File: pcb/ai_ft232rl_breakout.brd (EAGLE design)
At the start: 25.4 x 16.3 mm, 14 parts, among them U1 FT232RLSSOP

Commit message: aligned board to origin.
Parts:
- moved C1 35.6 mm to (18.8, 11.9)
- moved C2 35.6 mm to (18.0, 8.89)
- moved C3 35.6 mm to (17.3, 14.5)
- moved JP2 35.6 mm to (6.86, 1.78)
- moved LED1 35.6 mm to (20.1, 10.9)
- moved LED2 35.6 mm to (20.1, 7.87)
- moved PWR-LED 35.6 mm to (12.2, 2.03)
- moved PWRSEL 35.6 mm to (16.0, 1.52)
- moved R1 35.6 mm to (22.4, 11.2)
- moved R2 35.6 mm to (22.4, 8.13)
- moved R3 35.6 mm to (22.4, 5.08)
- moved R4 35.6 mm to (12.4, 4.83)
- moved U1 35.6 mm to (14.0, 9.14)
- moved USB 35.6 mm to (22.6, 8.13)

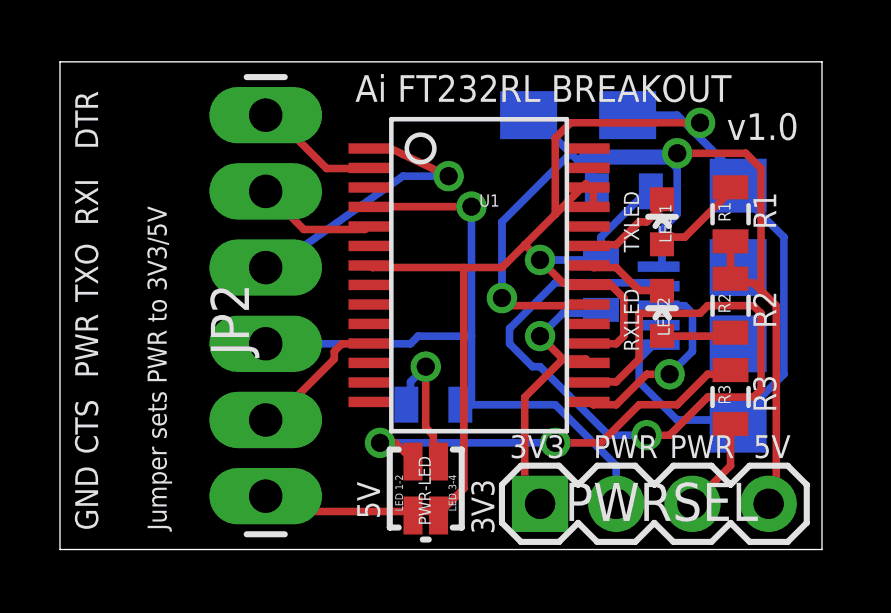
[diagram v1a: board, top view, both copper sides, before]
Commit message: re-routed manually, and changed components to use the Ai Eagle libraries.
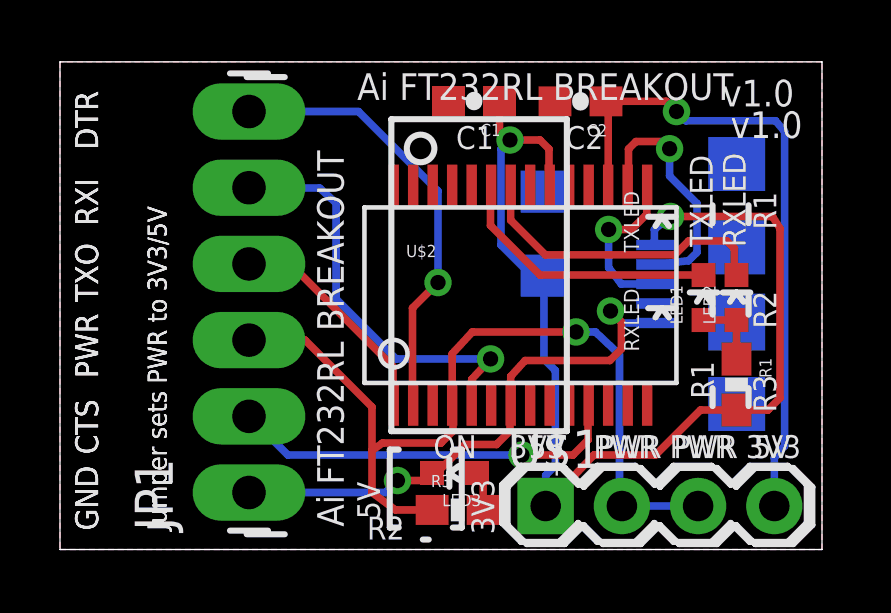
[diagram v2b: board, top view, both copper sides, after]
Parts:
- removed JP2: (no value), SparkFun-Connectors:1X06_LONGPADS
- removed PWR-LED: LED-BICOLOR, Acrobotic-LED:LED-BICOLOR-SMD
- removed PWRSEL: (no value), SparkFun-Connectors:1X04
- removed R2: 1K, SparkFun-Resistors:0805
- removed R4: 40, SparkFun-Resistors:0805
- removed U1: FT232RLSSOP, SparkFun-DigitalIC:SSOP28DB
- removed USB: USB-MICROB, SparkFun-Connectors:USB-MICROB
- added JP1: M06X1, Ai_Connectors:1X06-LONG
- added LED3: BLUE, Ai_LED:LED-0603
- added U$1: M04X1, Ai_Connectors:1X04
- added U$2: FT2332RL, Ai_IC:SSOP28-LD
- added USB1: USB-MICROB, Ai_Connectors:USB-MICROB
- C1, C2: device SparkFun-Capacitors:0805 -> Ai_Passives:0603-CAP
- C3: device SparkFun-Passives:EIA3216-KIT -> Ai_Passives:EIA3216
- LED1, LED2: device SparkFun-LED:LED-0603 -> Ai_LED:LED-0603
- R1: value 1K -> (none); device SparkFun-Resistors:0805 -> Ai_Passives:0603-RES
- R3: device SparkFun-Resistors:0805 -> Ai_Passives:0603-RES
- moved R3 9.84 mm to (13.3, 1.32), turned to 0 degrees
- moved C2 6.09 mm to (17.4, 14.9), flipped to the top, turned to 180 degrees
- moved C1 5.83 mm to (13.8, 14.9), flipped to the top
- moved R1 5.68 mm to (22.6, 5.50), turned to 270 degrees
- moved C3 4.10 mm to (16.2, 10.5), turned to 270 degrees
- moved LED1 2.88 mm to (21.5, 8.40)
- moved LED2 2.54 mm to (22.6, 8.40)
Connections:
- removed net N$11: PWR-LED.3, R4.1
- removed net N$5: LED2.A, R2.2
- removed net N$7: PWR-LED.1, R3.1
- removed net N$8: PWRSEL.3, R3.2
- new net N$9: LED3.A, R3.2
- net 3V3: now also U$1.4, U$2.17; no longer PWRSEL.1, U1.17
- net 5V: now also R1.2, U$1.1, U$2.20, USB1.VBUS; no longer PWRSEL.4, R1.1, R2.1, U1.20, USB.VBUS
- net CTS: now also JP1.2, U$2.11; no longer JP2.2, U1.11
- net DTR: now also JP1.6, U$2.2; no longer JP2.6, U1.2
- net GND: now also JP1.1, LED3.C, U$2.18, U$2.21, U$2.25, U$2.26, U$2.7, USB1.GND; no longer JP2.1, PWR-LED.2, PWR-LED.4, U1.18, U1.21, U1.25, U1.26, U1.7, USB.GND, USB.MT1, USB.MT2
- net N$1: now also U$2.23; no longer U1.23
- net N$2: now also U$2.22; no longer U1.22
- net N$3: now also U$2.16, USB1.D-; no longer U1.16, USB.D-
- net N$4: now also U$2.15, USB1.D+; no longer U1.15, USB.D+
- net N$6: now also LED2.A, R1.1; no longer R1.2
- net PWR: now also JP1.3, R3.1, U$1.2, U$1.3, U$2.4; no longer JP2.3, PWRSEL.2, R4.2, U1.4
- net RXI: now also JP1.5, U$2.5; no longer JP2.5, U1.5
- net TXO: now also JP1.4, U$2.1; no longer JP2.4, U1.1
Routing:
- net GND: track 63.4 -> 18.5 mm
- net N$3: track 26.8 -> 8.07 mm
- net N$7: track 14.1 -> 0.00 mm, vias 2 -> 0
- net 3V3: track 10.0 -> 21.8 mm
- net DTR: track 4.19 -> 14.9 mm, vias 0 -> 1
- net RXI: track 4.01 -> 14.1 mm, vias 0 -> 1
- net CTS: track 4.66 -> 13.3 mm, vias 0 -> 1
- net N$2: track 2.78 -> 10.3 mm
- net N$1: track 3.21 -> 9.13 mm
- net PWR: track 24.4 -> 29.4 mm
- net N$11: track 4.98 -> 0.00 mm, vias 1 -> 0
- net N$8: track 3.18 -> 0.00 mm
- net N$5: track 2.41 -> 0.00 mm
- net TXO: track 9.91 -> 7.51 mm, vias 1 -> 0
- net 5V: track 39.8 -> 37.7 mm
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- added copper zone on layer 1, net GND
- added copper zone on layer 16, net GND
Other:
- board text added: "C3"
- board text added: "ON"
